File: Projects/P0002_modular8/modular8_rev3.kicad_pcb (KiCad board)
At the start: 2 copper layers, 33 x 33 mm, 25 parts, among them IC1 ATMEGA328P-M, J1 modular8_rev3_comms_out, J2 modular8_rev3_comms_in, J3 modular8_rev3_interface_master, J4 modular8_rev3_interface_master, U1 LM4040D20IDBZR

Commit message: started routing modular8_rev3
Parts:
- C1, C5, C6: footprint Capacitors_SMD:C_0805 -> Capacitors_SMD:C_0603; moved to F.Cu
- C2, C3, C4: footprint Capacitors_SMD:C_0805 -> Capacitors_SMD:C_0603
- GC1, L1, R1, R2, R3, R4, R5: footprint Resistors_SMD:R_0805 -> Resistors_SMD:R_0603
- IC1: footprint Housings_QFP:TQFP-32_7x7mm_Pitch0.8mm -> Housings_DFN_QFN:QFN-32-1EP_5x5mm_Pitch0.5mm
- moved D2 20.4 mm to (163.7, 115.4)
- moved GC1 20.0 mm to (166.4, 107.4)
- moved R2 17.3 mm to (164.6, 121.0)
- moved R1 16.2 mm to (141.4, 107.6), turned to 0 degrees
- moved R5 14.0 mm to (129.2, 135.4)
- moved C6 13.3 mm to (135.8, 118.6)
- moved L1 11.5 mm to (138.8, 121.2)
- moved R4 11.3 mm to (135.6, 132.2)
- moved U1 10.8 mm to (146.3, 120.4)
- moved C4 10.7 mm to (143.1, 120.5)
- moved D1 10.3 mm to (137.1, 107.3), turned to 180 degrees
- moved XTAL?1 9.31 mm to (132.4, 116.8), turned to 270 degrees
- moved C5 9.10 mm to (133.5, 113.2), turned to 90 degrees
- moved C2 5.31 mm to (133.3, 107.8)
- moved R3 5.28 mm to (148.9, 122.9)
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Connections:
- C1 pad 1: Net-(C1-Pad1) -> +5V
- LDO1 pad 1: Net-(C1-Pad1) -> +5V
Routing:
- net +5V: track 9.64 -> 101.7 mm, vias 0 -> 9
- net /ABUS4/SDA: track 32.1 -> 0.00 mm, vias 2 -> 0
- net /MISO: track 28.2 -> 0.00 mm, vias 2 -> 0
- net /3V3: track 0.00 -> 26.3 mm, vias 0 -> 4
- net /TX: track 24.9 -> 0.00 mm, vias 2 -> 0
- net GND: track 0.00 -> 18.4 mm, vias 0 -> 5
- net /DBUS1: track 16.8 -> 0.00 mm, vias 2 -> 0
- net /DBUS4: track 15.9 -> 0.00 mm, vias 2 -> 0
- net /DBUS0: track 15.5 -> 0.00 mm, vias 1 -> 0
- net /SCK: track 14.6 -> 0.00 mm
- net /DBUS7: track 12.4 -> 0.00 mm, vias 3 -> 0
- net GNDA: track 0.00 -> 5.12 mm, vias 0 -> 1
- net Net-(C6-Pad1): track 0.33 -> 5.02 mm
- net /DBUS6: track 9.44 -> 13.3 mm
- net Net-(D2-Pad1): track 3.22 -> 0.00 mm
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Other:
- copper layers 2 -> 4
- net class BusV added: clearance 0.254, trace_width 0.1524, via_dia 0.508, via_drill 0.3302
- net class Default: clearance 0.2 -> 0.1524; trace_width 0.25 -> 0.1524; via_dia 0.6 -> 0.508; via_drill 0.4 -> 0.3302
- net class Power added: clearance 0.1524, trace_width 0.3048, via_dia 0.635, via_drill 0.4064
- rule trace_clearance: 0.2 -> 0.1524
- rule trace_min: 0.2 -> 0.1524
- rule via_min_drill: 0.3 -> 0.3302
- rule via_min_size: 0.4 -> 0.508

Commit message: first pass at routing
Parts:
- added REF**: modular8_mounting_hole, Libraries - KiCAD:modular8_mounting_hole, F.Cu at (152.4, 127.0)
- added REF**: modular8_mounting_hole, Libraries - KiCAD:modular8_mounting_hole, F.Cu at (127.0, 101.6)
- moved R5 30.9 mm to (141.2, 106.9)
- moved R4 23.4 mm to (141.4, 109.5)
- moved R2 22.6 mm to (145.3, 109.2), turned to 180 degrees
- moved GC1 21.4 mm to (145.3, 111.4)
- moved D2 20.3 mm to (145.3, 106.8), turned to 180 degrees
- moved C1 9.60 mm to (132.6, 106.7), turned to 0 degrees
- moved LDO1 9.13 mm to (132.8, 109.5)
- moved R3 8.26 mm to (144.3, 116.1), turned to 90 degrees
- moved L1 5.06 mm to (143.4, 119.0)
- moved R1 4.62 mm to (137.0, 109.2), turned to 180 degrees
- moved C2 4.50 mm to (132.6, 112.3), turned to 0 degrees
- moved U1 3.76 mm to (147.0, 116.7), turned to 270 degrees
- moved C4 2.80 mm to (145.9, 120.3)
- moved C3 2.31 mm to (147.0, 113.5), turned to 0 degrees
- moved C5 1.45 mm to (132.6, 114.3), turned to 180 degrees
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- renumbered XTAL?1 to 16MHz
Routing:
- net /ABUS4/SDA: track 0.00 -> 41.3 mm, vias 0 -> 2
- net /ABUS5/SCL: track 0.00 -> 37.2 mm, vias 0 -> 2
- net /MISO: track 0.00 -> 31.7 mm, vias 0 -> 3
- net /RX: track 0.00 -> 30.2 mm, vias 0 -> 2
- net /TX: track 0.00 -> 29.5 mm, vias 0 -> 2
- net /SCK: track 0.00 -> 25.9 mm, vias 0 -> 3
- net /MOSI: track 0.00 -> 24.9 mm, vias 0 -> 2
- net /DBUS1: track 0.00 -> 19.4 mm, vias 0 -> 2
- net GND: track 18.4 -> 37.6 mm, vias 5 -> 9
- net /DBUS0: track 0.00 -> 19.1 mm, vias 0 -> 1
- net /ABUS1: track 0.00 -> 13.7 mm, vias 0 -> 2
- net /ABUS3: track 0.00 -> 13.1 mm, vias 0 -> 2
- net /ABUS2: track 0.00 -> 12.8 mm, vias 0 -> 2
- net /DBUS7: track 0.00 -> 12.8 mm, vias 0 -> 1
- net /ABUS6*: track 0.00 -> 12.3 mm, vias 0 -> 1
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- added copper zone on In1.Cu, net GND
- added copper zone on In2.Cu, net GNDA
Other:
- board size 33 x 33 mm -> 30.5 x 30.5 mm

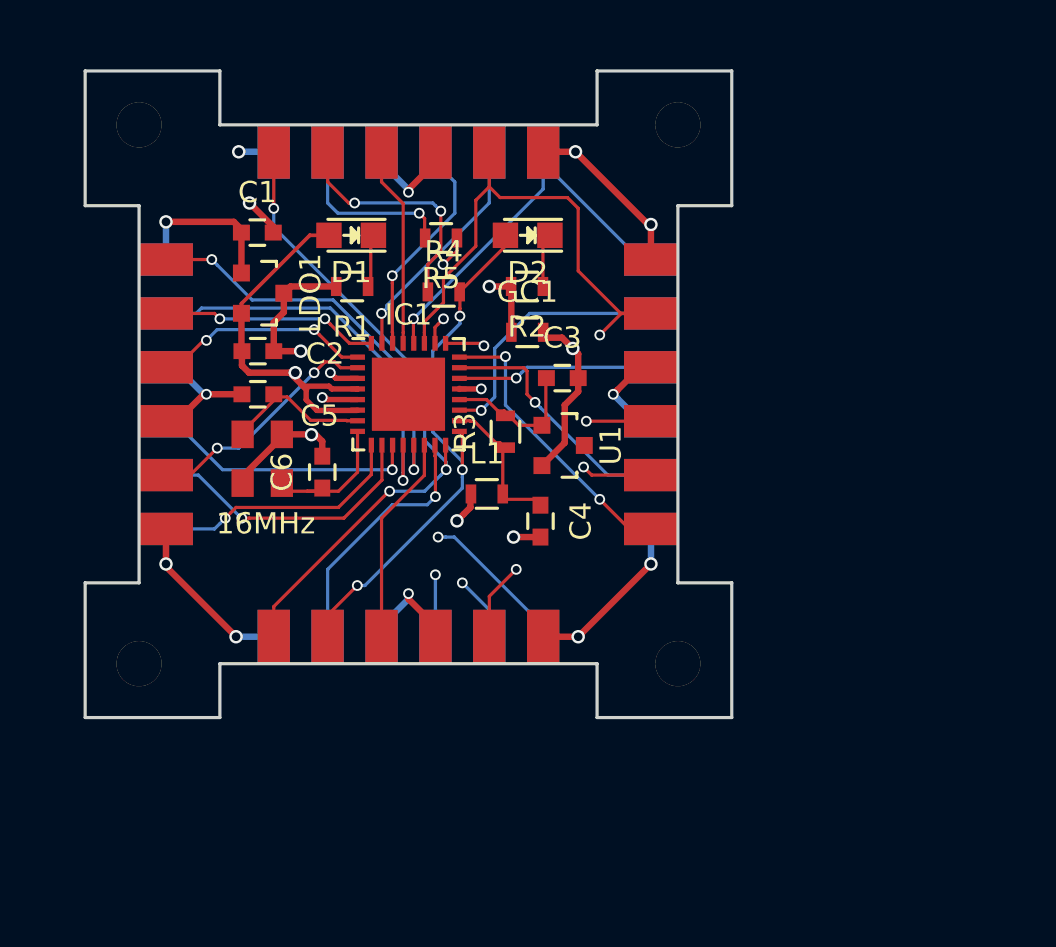
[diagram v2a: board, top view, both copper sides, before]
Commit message: fixed 1 unconnected
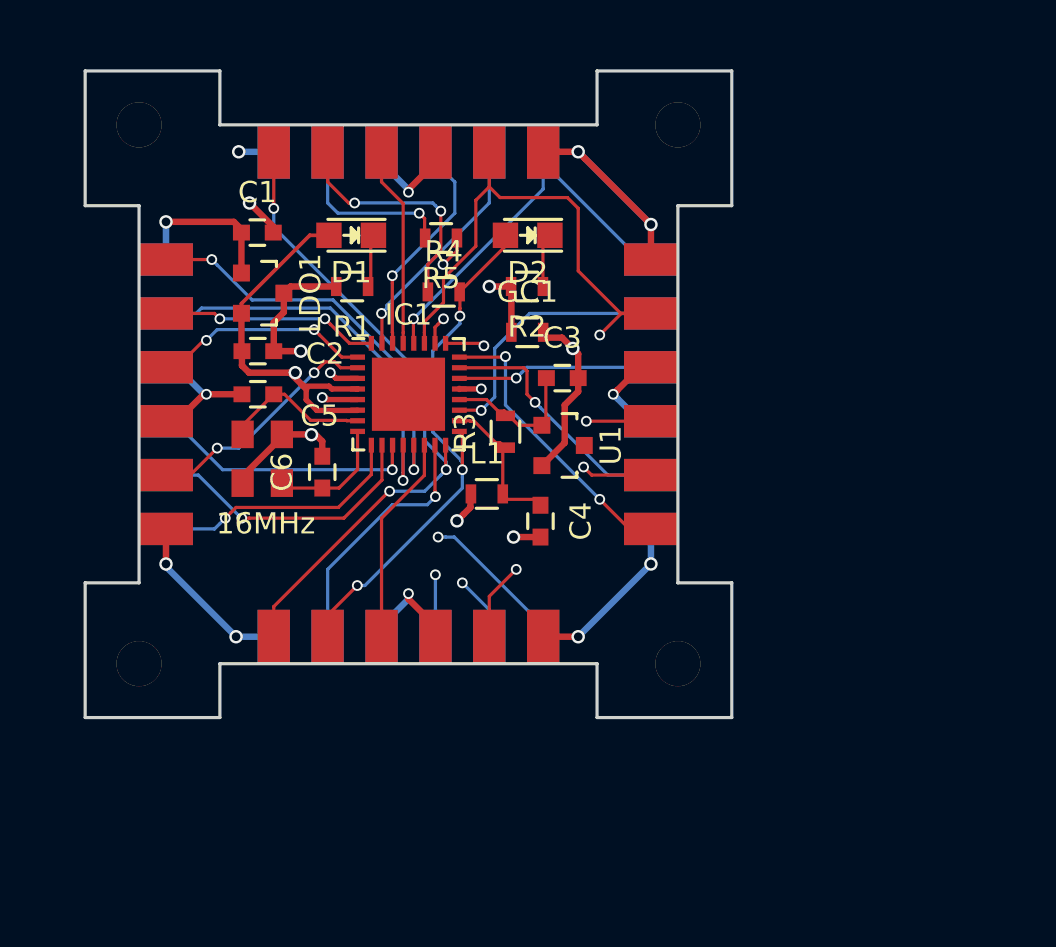
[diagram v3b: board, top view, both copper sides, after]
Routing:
- net +5V: track 97.9 -> 103.0 mm
- net Net-(C6-Pad1): track 7.59 -> 5.84 mm
